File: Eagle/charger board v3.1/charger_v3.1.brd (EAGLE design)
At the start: 98.7 x 90.2 mm, 42 parts, among them IC1 IR2110D, Q2 IRFP240, Q3 MJE13003G

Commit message: update board charger v3.1
update gnd lolipop
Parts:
- moved GND2 1.27 mm to (92.7, 26.7)
- moved P_5V 1.27 mm to (92.7, 33.0)
- moved GND1 1.27 mm to (92.7, 24.1)
- moved P_3V3 1.27 mm to (92.7, 39.4)
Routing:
- net GND: track 652.4 -> 407.8 mm, vias 5 -> 0
- net PWM_12V: track 147.0 -> 102.9 mm
- net NMOS_SOURCE: track 226.4 -> 188.4 mm, vias 4 -> 2
- net N$14: track 53.7 -> 49.0 mm
- net V_OUT: track 69.4 -> 67.3 mm
- net PWM_SW1: track 52.6 -> 51.1 mm
- net PWM_5V: track 66.8 -> 67.9 mm

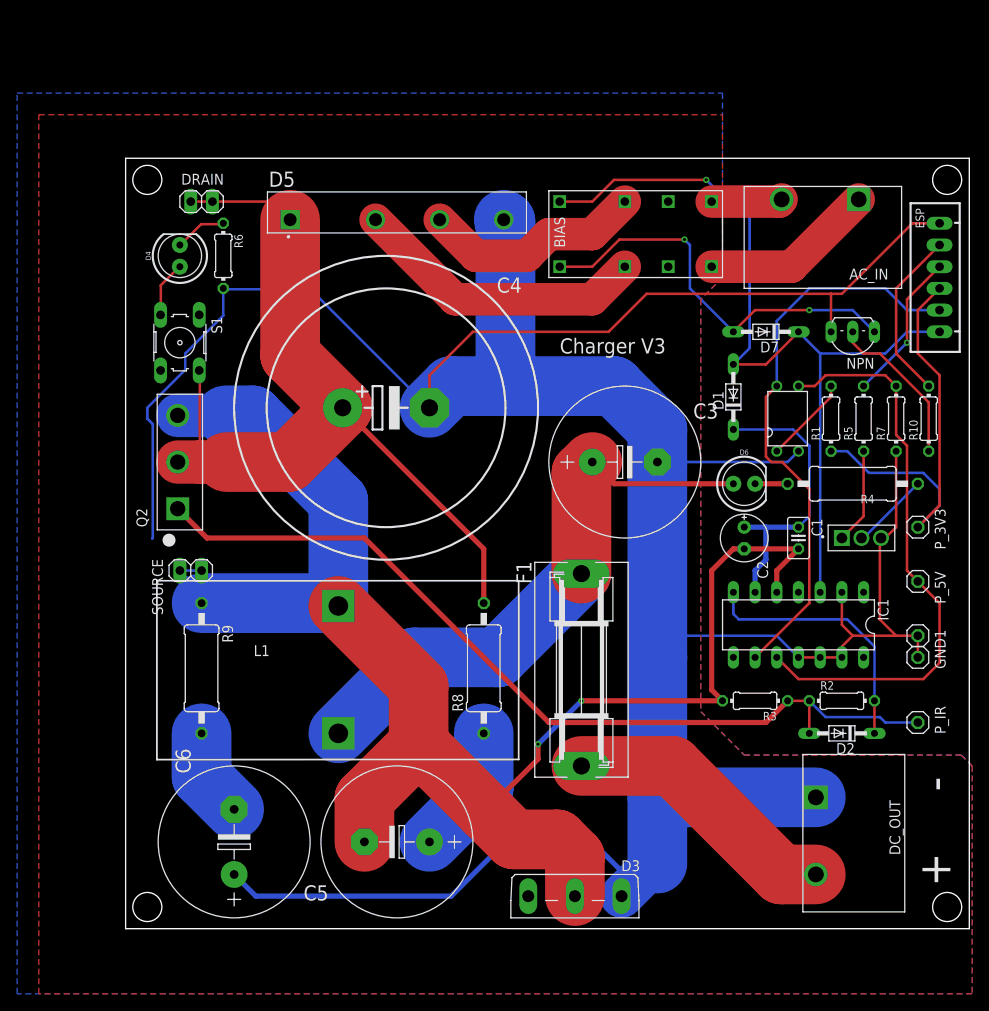
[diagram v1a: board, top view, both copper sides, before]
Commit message: update chg v3.1
relay ganti jadi songle 1ch lagi
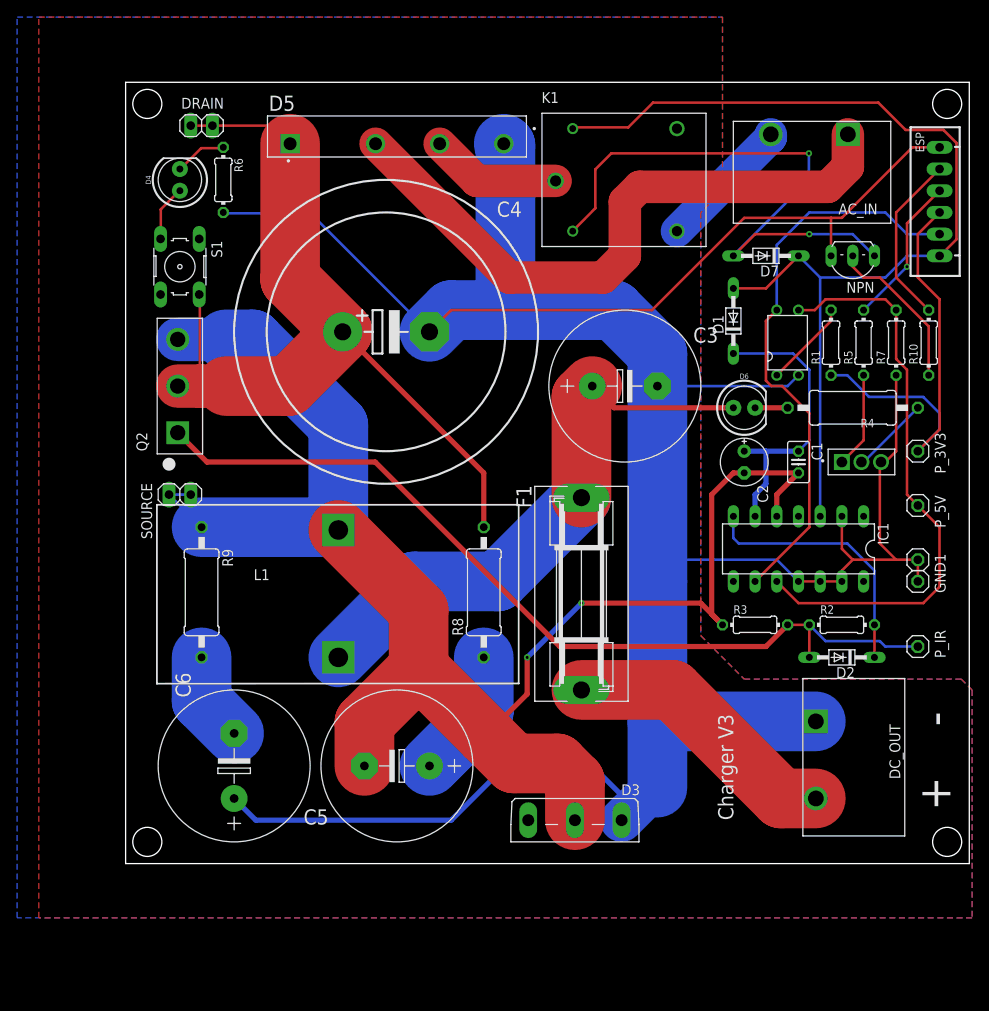
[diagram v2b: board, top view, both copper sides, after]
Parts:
- removed U$1: DPDT-HK19F, TA_library:DPDT-HK19F
- added K1: SRD-12VDC-SL-C, TA_library:RELAY_SRD-12VDC-SL-C
- moved SOURCE 8.98 mm to (6.35, 43.2)
- moved D7 8.89 mm to (74.9, 71.1)
- moved NPN 8.89 mm to (85.1, 71.1)
- moved GND1 8.89 mm to (92.7, 33.0)
- moved C1 8.89 mm to (78.7, 47.0)
- moved C2 8.89 mm to (72.4, 47.0)
- moved C3 8.89 mm to (58.4, 55.9)
- moved C5 8.89 mm to (31.8, 11.4)
- moved C6 8.89 mm to (12.7, 11.4)
- moved D1 8.89 mm to (71.1, 63.5)
- moved D3 8.89 mm to (52.6, 2.54)
- moved D4 8.89 mm to (6.35, 80.0)
- moved D5 8.89 mm to (31.8, 85.1)
- moved D6 8.89 mm to (72.4, 53.3)
- moved DC_OUT 8.89 mm to (86.1, 13.4)
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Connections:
- removed net AC_IN_2: AC_IN.1, U$1.2
- net 12V: now also K1.COIL1; no longer U$1.7
- net AC_1: now also K1.COM; no longer U$1.5
- net AC_2: now also AC_IN.1; no longer U$1.6
- net AC_IN_1: now also K1.NO; no longer U$1.1
- net N$14: now also K1.COIL2; no longer U$1.8
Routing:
- net AC_2: track 34.6 -> 74.7 mm
- net GND: track 407.8 -> 368.6 mm
- net N$14: track 49.0 -> 69.6 mm
- net AC_IN_2: track 20.5 -> 0.00 mm
- net 12V: track 98.8 -> 118.0 mm, vias 1 -> 0
- net AC_1: track 26.1 -> 15.4 mm
- net AC_IN_1: track 8.29 -> 15.9 mm
- net NMOS_SOURCE: track 188.4 -> 192.5 mm
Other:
- board size 98.7 x 90.2 mm -> 98.7 x 91.4 mm

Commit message: update chg v3.1
benerin airwire, stubs
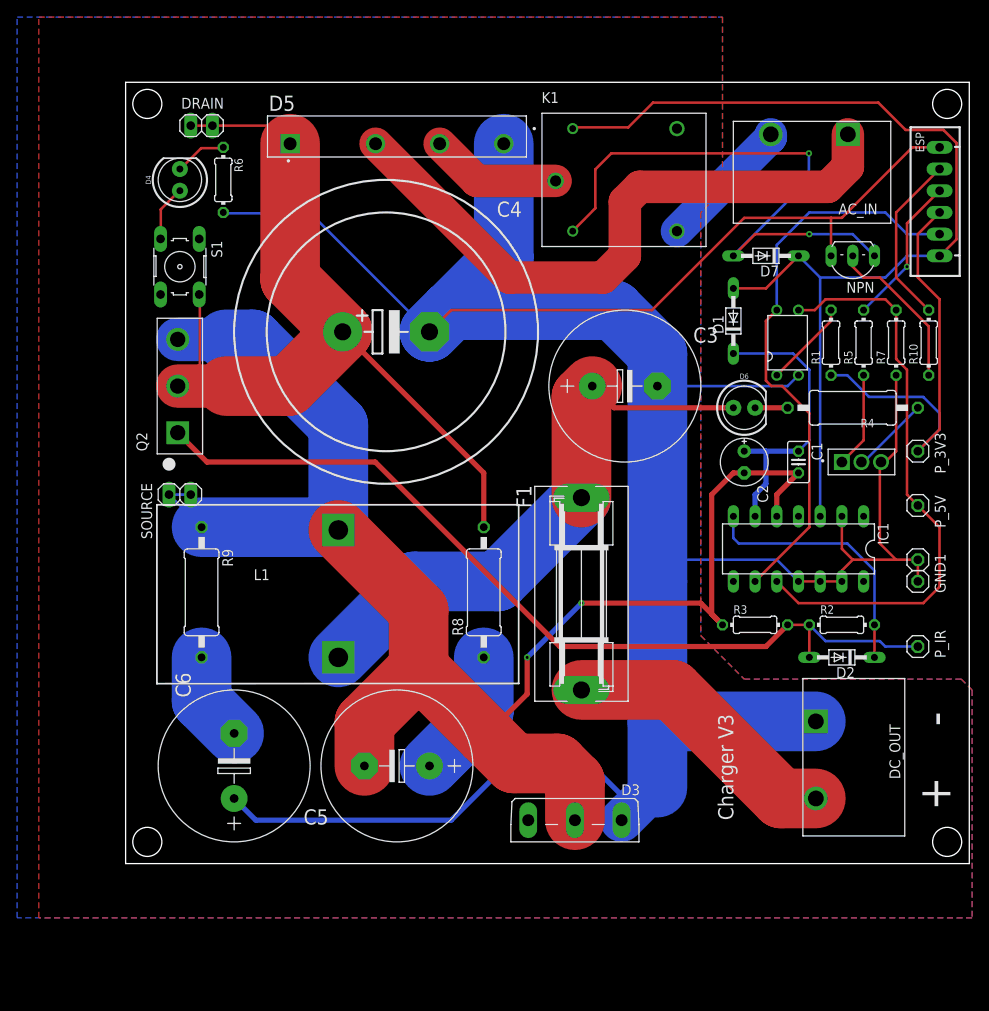
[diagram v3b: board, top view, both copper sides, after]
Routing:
- net GND: track 368.6 -> 370.1 mm
- net HVDC: track 101.9 -> 100.7 mm
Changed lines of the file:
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@@
 <drawing>
 <settings>
-<setting alwaysvectorfont="yes"/>
+<setting alwaysvectorfont="no"/>
 <setting verticaltext="up"/>
 </settings>
@@
 <wire x1="21.6408" y1="76.0984" x2="35.5092" y2="62.23" width="0.3048" layer="16"/>
 <wire x1="35.5092" y1="62.23" x2="35.56" y2="62.23" width="0.3048" layer="16"/>
-<wire x1="44.196" y1="84.1756" x2="44.25" y2="84.24" width="0.3048" layer="16"/>
-<wire x1="35.6616" y1="62.23" x2="35.56" y2="62.23" width="0.3048" layer="1"/>
-<wire x1="58.039" y1="5.08" x2="58.039" y2="7.5184" width="0.3048" layer="16"/>
 <wire x1="12.8016" y1="7.5184" x2="12.7" y2="7.62" width="0.3048" layer="16"/>
-<wire x1="58.039" y1="5.08" x2="61.849" y2="8.89" width="5.08" layer="16"/>
+<wire x1="61.849" y1="8.89" x2="58.039" y2="5.08" width="5.08" layer="16"/>
 <wire x1="61.849" y1="8.89" x2="62.23" y2="8.89" width="5.08" layer="16"/>
 <wire x1="35.56" y1="62.23" x2="38.1" y2="64.77" width="6.985" layer="16"/>
-<wire x1="44.45" y1="64.77" x2="38.1" y2="64.77" width="6.985" layer="16"/>
-<wire x1="44.25" y1="84.24" x2="44.45" y2="84.04" width="6.985" layer="16"/>
-<wire x1="44.45" y1="84.04" x2="44.45" y2="64.77" width="6.985" layer="16"/>
 <contactref element="D3" pad="A1"/>
 <contactref element="IC1" pad="2"/>
@@
 <contactref element="IC1" pad="12"/>
 <contactref element="IC1" pad="13"/>
-<wire x1="58.039" y1="5.08" x2="58.039" y2="8.001" width="0.6096" layer="16"/>
 <wire x1="58.039" y1="8.001" x2="54.61" y2="11.43" width="0.6096" layer="16"/>
 <wire x1="54.61" y1="11.43" x2="44.45" y2="11.43" width="0.6096" layer="16"/>
@@
 <wire x1="57.15" y1="64.77" x2="62.23" y2="59.69" width="6.985" layer="16"/>
 <wire x1="62.23" y1="59.69" x2="62.23" y2="55.88" width="6.985" layer="16"/>
-<wire x1="44.45" y1="64.77" x2="57.15" y2="64.77" width="6.985" layer="16"/>
+<wire x1="38.1" y1="64.77" x2="57.15" y2="64.77" width="6.985" layer="16"/>
 <wire x1="62.23" y1="8.89" x2="62.23" y2="16.51" width="6.985" layer="16"/>
 <contactref element="NPN" pad="E"/>
@@
 <wire x1="82.55" y1="75.565" x2="82.55" y2="71.12" width="0.3048" layer="1"/>
 <wire x1="11.43" y1="76.2" x2="11.43" y2="76.0984" width="0.3048" layer="16"/>
-<wire x1="35.56" y1="60.325" x2="35.56" y2="62.23" width="0.3048" layer="1"/>
 <wire x1="35.56" y1="62.23" x2="38.1" y2="64.77" width="0.3048" layer="1"/>
 <wire x1="62.23" y1="33.02" x2="64.77" y2="35.56" width="0.3048" layer="16"/>
@@
 <wire x1="83.82" y1="36.83" x2="85.09" y2="35.56" width="0.3048" layer="1"/>
 <wire x1="85.09" y1="35.56" x2="90.17" y2="35.56" width="0.3048" layer="1"/>
+<wire x1="58.039" y1="5.08" x2="58.039" y2="8.001" width="0.3048" layer="16"/>
+<wire x1="44.25" y1="84.24" x2="44.25" y2="70.92" width="6.985" layer="16"/>
+<wire x1="44.25" y1="70.92" x2="35.56" y2="62.23" width="6.985" layer="16"/>
 </signal>
 <signal name="5V">
@@
 <wire x1="41.91" y1="45.72" x2="41.91" y2="39.37" width="0.6096" layer="1"/>
 <wire x1="25.4" y1="62.23" x2="41.91" y2="45.72" width="0.6096" layer="1"/>
-<wire x1="8.6868" y1="55.88" x2="8.6868" y2="58.26125" width="0.3048" layer="1"/>
 <wire x1="8.6868" y1="58.26125" x2="8.6868" y2="66.4972" width="0.3048" layer="1"/>
 <wire x1="8.6868" y1="66.4972" x2="8.6106" y2="66.5988" width="0.3048" layer="1"/>
 <wire x1="11.811" y1="55.88" x2="19.05" y2="55.88" width="6.985" layer="1"/>
-<wire x1="6.095" y1="55.88" x2="8.73125" y2="55.88" width="5.08" layer="1"/>
-<wire x1="8.73125" y1="55.88" x2="11.811" y2="55.88" width="5.08" layer="1"/>
+<wire x1="6.095" y1="55.88" x2="11.811" y2="55.88" width="5.08" layer="1"/>
 <wire x1="8.73125" y1="58.26125" x2="8.6868" y2="58.26125" width="0.3048" layer="1"/>
-<wire x1="8.73125" y1="58.26125" x2="8.73125" y2="55.88" width="0.3048" layer="1"/>
 <contactref element="Q2" pad="2"/>
 <contactref element="DRAIN" pad="1"/>
@@
 <contactref element="DRAIN" pad="2"/>
 <wire x1="7.62" y1="86.36" x2="10.16" y2="86.36" width="0.3048" layer="1"/>
+<wire x1="6.095" y1="55.88" x2="8.47625" y2="58.26125" width="0.3048" layer="1"/>
+<wire x1="8.47625" y1="58.26125" x2="8.6868" y2="58.26125" width="0.3048" layer="1"/>
 </signal>
 <signal name="12V">
